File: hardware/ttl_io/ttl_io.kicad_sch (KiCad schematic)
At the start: 0 parts

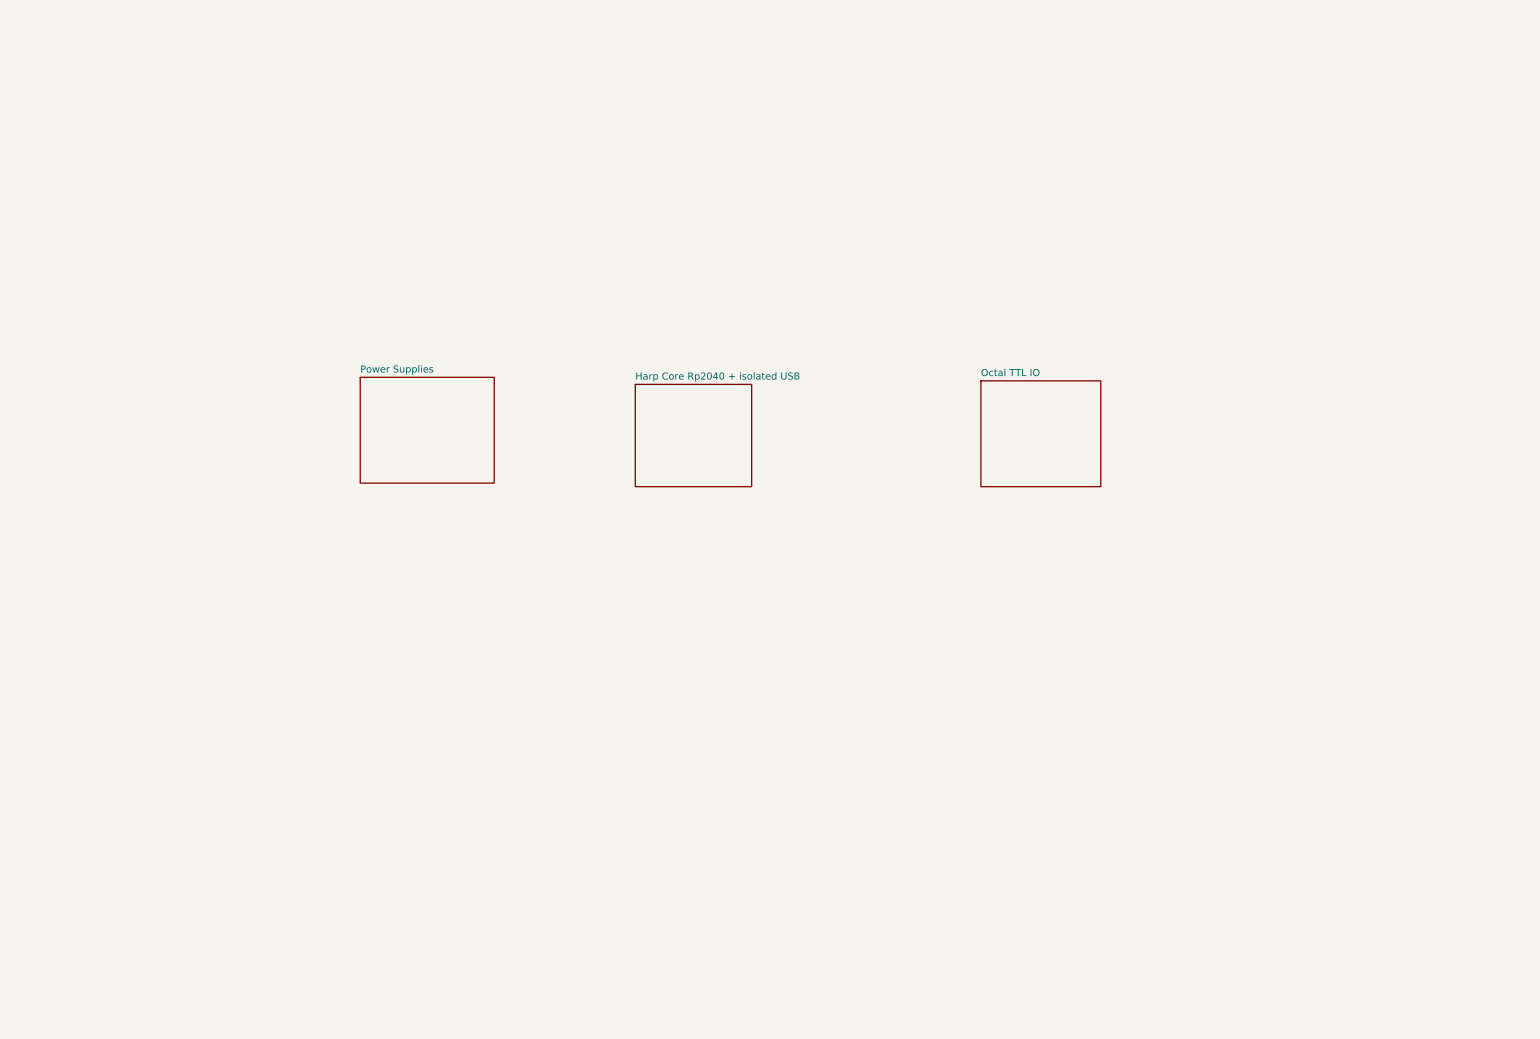
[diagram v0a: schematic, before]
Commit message: draft mcu bypass with bus switches
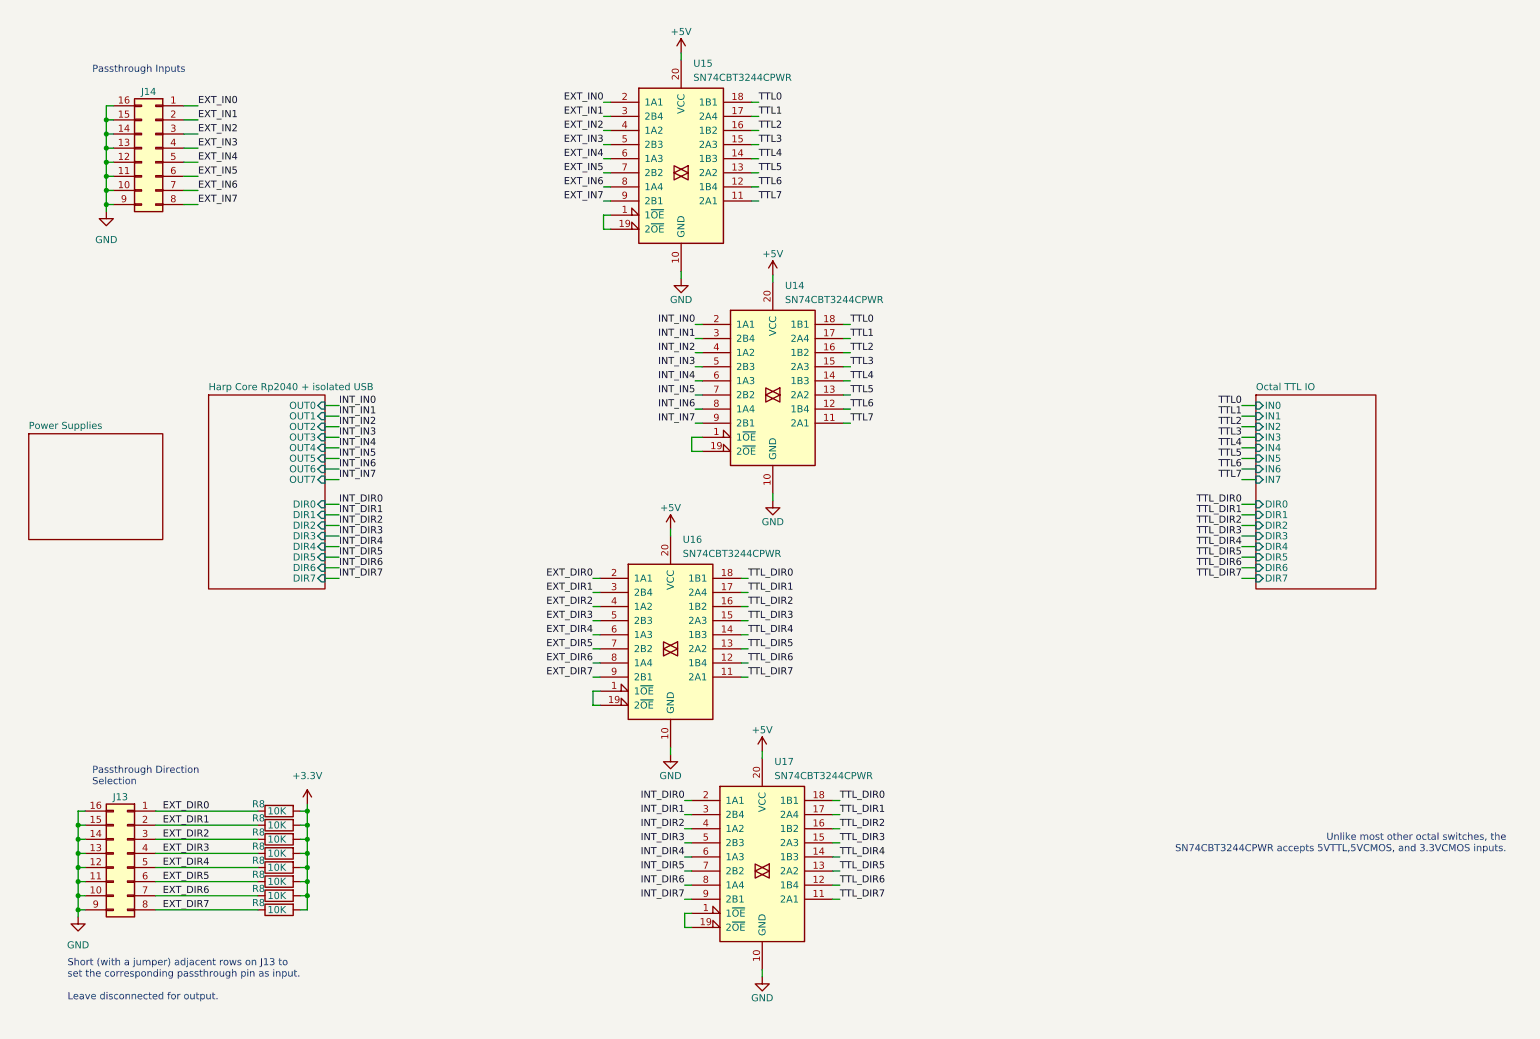
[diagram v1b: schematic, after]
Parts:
- added J13, J14: Conn_02x08_Counter_Clockwise, symbol Connector_Generic:Conn_02x08_Counter_Clockwise
- added R8 (x8): 10K, Resistor_SMD:R_0402_1005Metric, symbol Device:R
- added U14, U15, U16, U17: SN74CBT3244CPWR, Package_SO:TSSOP-20_4.4x6.5mm_P0.65mm, symbol kicad_component_library:SN74CBT3244CPWR
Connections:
- new net: U14.1 (1~{OE}), U14.19 (2~{OE})
- new net: U16.1 (1~{OE}), U16.19 (2~{OE})
- new net: U17.1 (1~{OE}), U17.19 (2~{OE})
- new net: U15.1 (1~{OE}), U15.19 (2~{OE})
- new net +3V3: R8.2, R8.2, R8.2, R8.2, R8.2, R8.2, R8.2, R8.2
- new net +5V: U14.20 (VCC), U15.20 (VCC), U16.20 (VCC), U17.20 (VCC)
- new net EXT_DIR0: J13.1 (Pin_1), R8.1, U16.2 (1A1)
- new net EXT_DIR1: J13.2 (Pin_2), R8.1, U16.3 (2B4)
- new net EXT_DIR2: J13.3 (Pin_3), R8.1, U16.4 (1A2)
- new net EXT_DIR3: J13.4 (Pin_4), R8.1, U16.5 (2B3)
- new net EXT_DIR4: J13.5 (Pin_5), R8.1, U16.6 (1A3)
- new net EXT_DIR5: J13.6 (Pin_6), R8.1, U16.7 (2B2)
- new net EXT_DIR6: J13.7 (Pin_7), R8.1, U16.8 (1A4)
- new net EXT_DIR7: J13.8 (Pin_8), R8.1, U16.9 (2B1)
- new net EXT_IN0: J14.1 (Pin_1), U15.2 (1A1)
- new net EXT_IN1: J14.2 (Pin_2), U15.3 (2B4)
- new net EXT_IN2: J14.3 (Pin_3), U15.4 (1A2)
- new net EXT_IN3: J14.4 (Pin_4), U15.5 (2B3)
- new net EXT_IN4: J14.5 (Pin_5), U15.6 (1A3)
- new net EXT_IN5: J14.6 (Pin_6), U15.7 (2B2)
- new net EXT_IN6: J14.7 (Pin_7), U15.8 (1A4)
- new net EXT_IN7: J14.8 (Pin_8), U15.9 (2B1)
- new net GND: J13.10 (Pin_10), J13.11 (Pin_11), J13.12 (Pin_12), J13.13 (Pin_13), J13.14 (Pin_14), J13.15 (Pin_15), J13.16 (Pin_16), J13.9 (Pin_9), J14.10 (Pin_10), J14.11 (Pin_11), J14.12 (Pin_12), J14.13 (Pin_13), J14.14 (Pin_14), J14.15 (Pin_15), J14.16 (Pin_16), J14.9 (Pin_9), U14.10 (GND), U15.10 (GND), U16.10 (GND), U17.10 (GND)
- new net INT_DIR0: U17.2 (1A1)
- new net INT_DIR1: U17.3 (2B4)
- new net INT_DIR2: U17.4 (1A2)
- new net INT_DIR3: U17.5 (2B3)
- new net INT_DIR4: U17.6 (1A3)
- new net INT_DIR5: U17.7 (2B2)
- new net INT_DIR6: U17.8 (1A4)
- new net INT_DIR7: U17.9 (2B1)
- new net INT_IN0: U14.2 (1A1)
- new net INT_IN1: U14.3 (2B4)
- new net INT_IN2: U14.4 (1A2)
- new net INT_IN3: U14.5 (2B3)
- new net INT_IN4: U14.6 (1A3)
- new net INT_IN5: U14.7 (2B2)
- new net INT_IN6: U14.8 (1A4)
- new net INT_IN7: U14.9 (2B1)
- new net TTL0: U14.18 (1B1), U15.18 (1B1)
- new net TTL1: U14.17 (2A4), U15.17 (2A4)
- new net TTL2: U14.16 (1B2), U15.16 (1B2)
- new net TTL3: U14.15 (2A3), U15.15 (2A3)
- new net TTL4: U14.14 (1B3), U15.14 (1B3)
- new net TTL5: U14.13 (2A2), U15.13 (2A2)
- new net TTL6: U14.12 (1B4), U15.12 (1B4)
- new net TTL7: U14.11 (2A1), U15.11 (2A1)
- new net TTL_DIR0: U16.18 (1B1), U17.18 (1B1)
- new net TTL_DIR1: U16.17 (2A4), U17.17 (2A4)
- new net TTL_DIR2: U16.16 (1B2), U17.16 (1B2)
- new net TTL_DIR3: U16.15 (2A3), U17.15 (2A3)
- new net TTL_DIR4: U16.14 (1B3), U17.14 (1B3)
- new net TTL_DIR5: U16.13 (2A2), U17.13 (2A2)
- new net TTL_DIR6: U16.12 (1B4), U17.12 (1B4)
- new net TTL_DIR7: U16.11 (2A1), U17.11 (2A1)
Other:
- sheet Harp Core Rp2040 + isolated USB ports: added DIR0, DIR1, DIR2, DIR3, DIR4, DIR5, DIR6, DIR7, OUT0, OUT1, OUT2, OUT3, OUT4, OUT5, OUT6, OUT7; removed none
- sheet Octal TTL IO ports: added DIR0, DIR1, DIR2, DIR3, DIR4, DIR5, DIR6, DIR7, IN0, IN1, IN2, IN3, IN4, IN5, IN6, IN7; removed none
- note added: "Passthrough Direction Selection"
- note added: "Passthrough Inputs"
- note added: "Short (with a jumper) adjacent rows on J13 to set the corresponding passthrough pin as input. Leave disconnected for output."
- note added: "Unlike most other octal switches, the SN74CBT3244CPWR accepts 5VTTL,5VCMOS, and 3.3VCMOS inputs."

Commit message: update schematic with bus switches
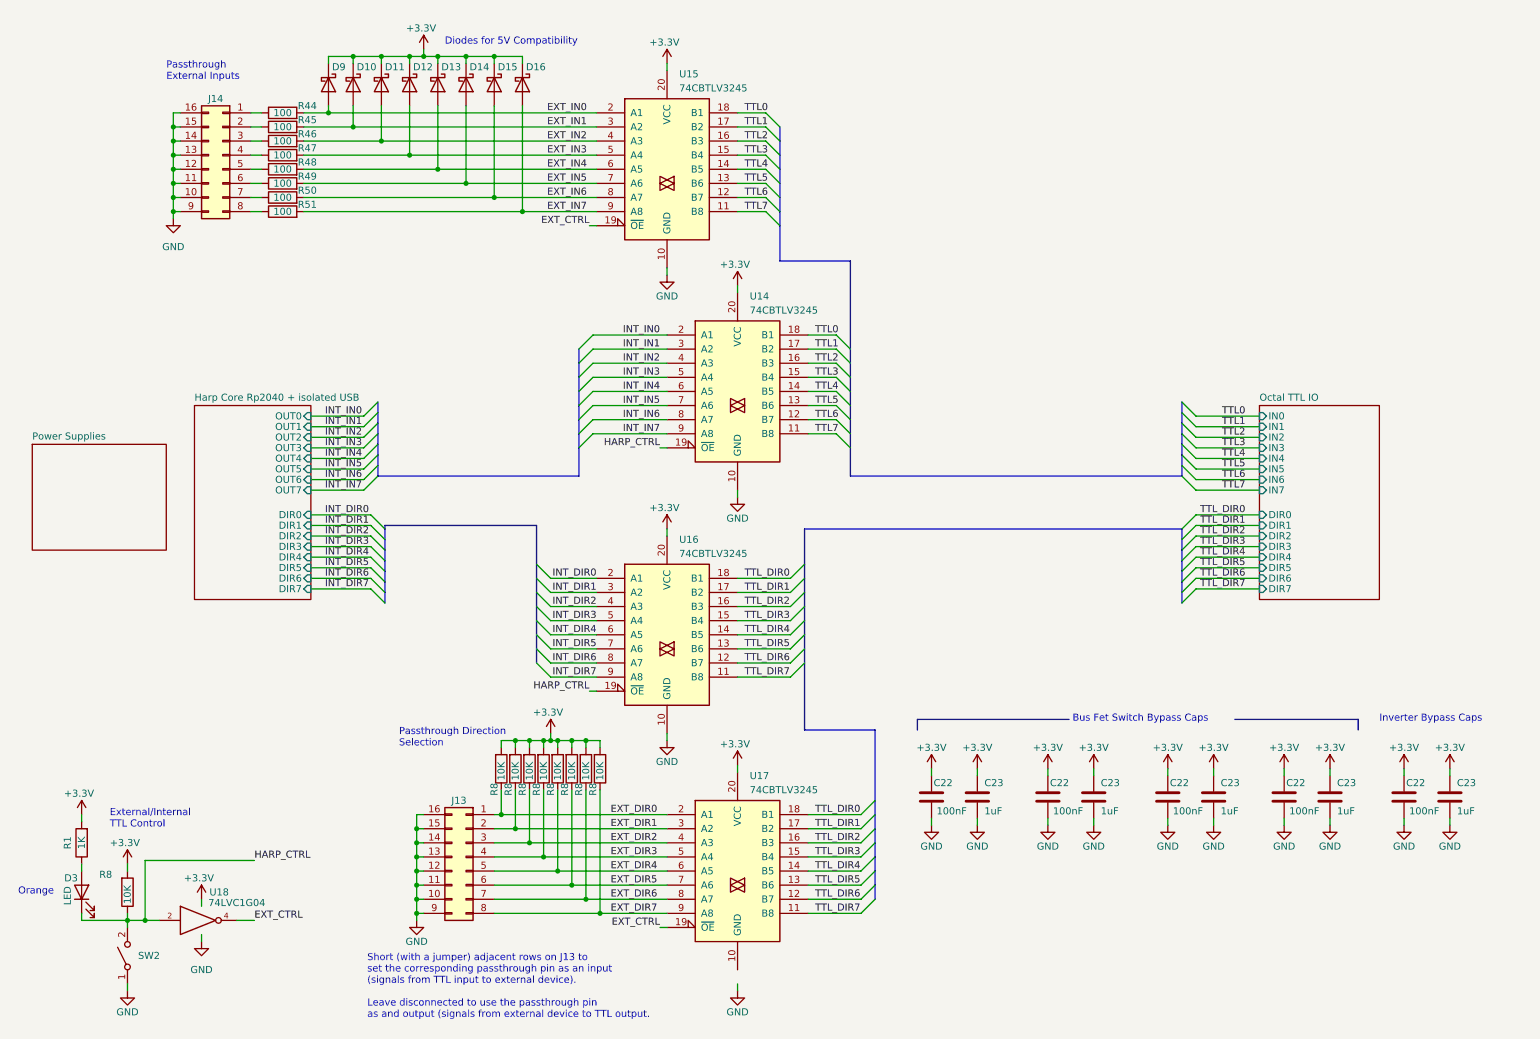
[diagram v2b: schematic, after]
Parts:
- removed U14, U15, U16, U17: SN74CBT3244CPWR, Package_SO:TSSOP-20_4.4x6.5mm_P0.65mm, symbol kicad_component_library:SN74CBT3244CPWR
- added C22 (x5): 100nF, Capacitor_SMD:C_0402_1005Metric, symbol Device:C
- added C23 (x5): 1uF, Capacitor_SMD:C_0402_1005Metric, symbol Device:C
- added D10, D11, D12, D13, D14, D15, D16, D9: D_Schottky, Diode_SMD:D_SOD-123, symbol Device:D_Schottky
- added D3: LED, LED_SMD:LED_0603_1608Metric, symbol Device:LED
- added R1: 1K, Resistor_SMD:R_0402_1005Metric, symbol Device:R
- added R44, R45, R46, R47, R48, R49, R50, R51: 100, symbol Device:R
- added R8: 10K, Resistor_SMD:R_0402_1005Metric, symbol Device:R
- added SW2: SW_SPST, symbol Switch:SW_SPST
- added U14, U15, U16, U17: 74CBTLV3245, Package_SO:TSSOP-20_4.4x6.5mm_P0.65mm, symbol kicad_component_library:74CBTLV3245
- added U18: 74LVC1G04, symbol 74xGxx:74LVC1G04
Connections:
- net +3V3: now also C22.2, C22.2, C22.2, C22.2, C22.2, C23.1, C23.1, C23.1, C23.1, C23.1, D10.1 (K), D11.1 (K), D12.1 (K), D13.1 (K), D14.1 (K), D15.1 (K), D16.1 (K), D9.1 (K), R1.2, R8.2, U14.20 (VCC), U15.20 (VCC), U16.20 (VCC), U17.20 (VCC), U18.5 (VCC)
- net EXT_DIR0: now also U17.2 (A1)
- net EXT_DIR1: now also U17.3 (A2)
- net EXT_DIR2: now also U17.4 (A3)
- net EXT_DIR3: now also U17.5 (A4)
- net EXT_DIR4: now also U17.6 (A5)
- net EXT_DIR5: now also U17.7 (A6)
- net EXT_DIR6: now also U17.8 (A7)
- net EXT_DIR7: now also U17.9 (A8)
- net EXT_IN0: now also D9.2 (A), R44.2, U15.2 (A1); no longer J14.1 (Pin_1)
- net EXT_IN1: now also D10.2 (A), R45.2, U15.3 (A2); no longer J14.2 (Pin_2)
- net EXT_IN2: now also D11.2 (A), R46.2, U15.4 (A3); no longer J14.3 (Pin_3)
- net EXT_IN3: now also D12.2 (A), R47.2, U15.5 (A4); no longer J14.4 (Pin_4)
- net EXT_IN4: now also D13.2 (A), R48.2, U15.6 (A5); no longer J14.5 (Pin_5)
- net EXT_IN5: now also D14.2 (A), R49.2, U15.7 (A6); no longer J14.6 (Pin_6)
- net EXT_IN6: now also D15.2 (A), R50.2, U15.8 (A7); no longer J14.7 (Pin_7)
- net EXT_IN7: now also D16.2 (A), R51.2, U15.9 (A8); no longer J14.8 (Pin_8)
- net GND: now also C22.1, C22.1, C22.1, C22.1, C22.1, C23.2, C23.2, C23.2, C23.2, C23.2, SW2.1 (A), U14.10 (GND), U15.10 (GND), U16.10 (GND), U18.3 (GND)
- net INT_DIR0: now also U16.2 (A1)
- net INT_DIR1: now also U16.3 (A2)
- net INT_DIR2: now also U16.4 (A3)
- net INT_DIR3: now also U16.5 (A4)
- net INT_DIR4: now also U16.6 (A5)
- net INT_DIR5: now also U16.7 (A6)
- net INT_DIR6: now also U16.8 (A7)
- net INT_DIR7: now also U16.9 (A8)
- net INT_IN0: now also U14.2 (A1)
- net INT_IN1: now also U14.3 (A2)
- net INT_IN2: now also U14.4 (A3)
- net INT_IN3: now also U14.5 (A4)
- net INT_IN4: now also U14.6 (A5)
- net INT_IN5: now also U14.7 (A6)
- net INT_IN6: now also U14.8 (A7)
- net INT_IN7: now also U14.9 (A8)
- net TTL0: now also U14.18 (B1), U15.18 (B1)
- net TTL1: now also U14.17 (B2), U15.17 (B2)
- net TTL2: now also U14.16 (B3), U15.16 (B3)
- net TTL3: now also U14.15 (B4), U15.15 (B4)
- net TTL4: now also U14.14 (B5), U15.14 (B5)
- net TTL5: now also U14.13 (B6), U15.13 (B6)
- net TTL6: now also U14.12 (B7), U15.12 (B7)
- net TTL7: now also U14.11 (B8), U15.11 (B8)
- net TTL_DIR0: now also U16.18 (B1), U17.18 (B1)
- net TTL_DIR1: now also U16.17 (B2), U17.17 (B2)
- net TTL_DIR2: now also U16.16 (B3), U17.16 (B3)
- net TTL_DIR3: now also U16.15 (B4), U17.15 (B4)
- net TTL_DIR4: now also U16.14 (B5), U17.14 (B5)
- net TTL_DIR5: now also U16.13 (B6), U17.13 (B6)
- net TTL_DIR6: now also U16.12 (B7), U17.12 (B7)
- net TTL_DIR7: now also U16.11 (B8), U17.11 (B8)
- new net: J14.7 (Pin_7), R50.1
- new net: J14.1 (Pin_1), R44.1
- new net: J14.2 (Pin_2), R45.1
- new net: J14.3 (Pin_3), R46.1
- new net: J14.4 (Pin_4), R47.1
- new net: J14.5 (Pin_5), R48.1
- new net: J14.6 (Pin_6), R49.1
- new net: J14.8 (Pin_8), R51.1
- new net: D3.2 (A), R1.1
- new net EXT_CTRL: U15.19 (~{OE}), U17.19 (~{OE}), U18.4
- new net HARP_CTRL: D3.1 (K), R8.1, SW2.2 (B), U14.19 (~{OE}), U16.19 (~{OE}), U18.2
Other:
- note added: "Bus Fet Switch Bypass Caps"
- note added: "Diodes for 5V Compatibility"
- note added: "External/Internal TTL Control"
- note added: "Inverter Bypass Caps"
- note added: "Orange"
- note added: "Passthrough External Inputs"
- note added: "Short (with a jumper) adjacent rows on J13 to set the corresponding passthrough pin as an input (signals from TTL input to external device). Leave disconnected to use the passthrough pin as and output (signals from external device to TTL output."
- note removed: "Passthrough Inputs"
- note removed: "Short (with a jumper) adjacent rows on J13 to set the corresponding passthrough pin as input. Leave disconnected for output."
- note removed: "Unlike most other octal switches, the SN74CBT3244CPWR accepts 5VTTL,5VCMOS, and 3.3VCMOS inputs."
- moved on the sheet: J13, J14, R8
